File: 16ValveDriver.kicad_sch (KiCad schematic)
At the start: 0 parts

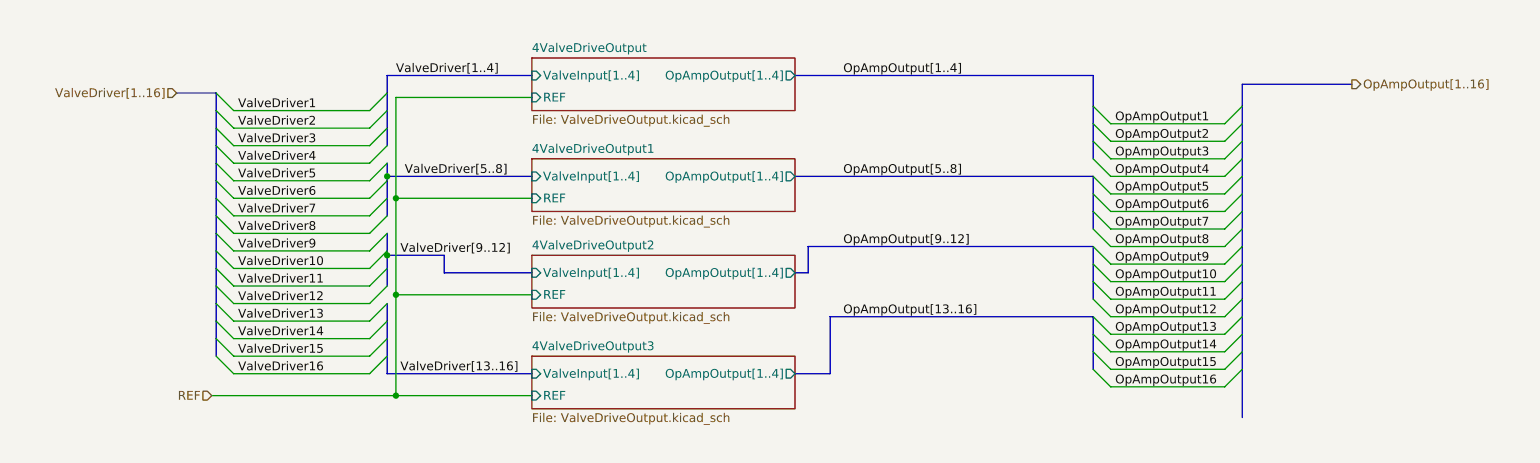
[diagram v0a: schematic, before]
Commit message: Layout p2, fix Analog VCC and GND for opamp circuit
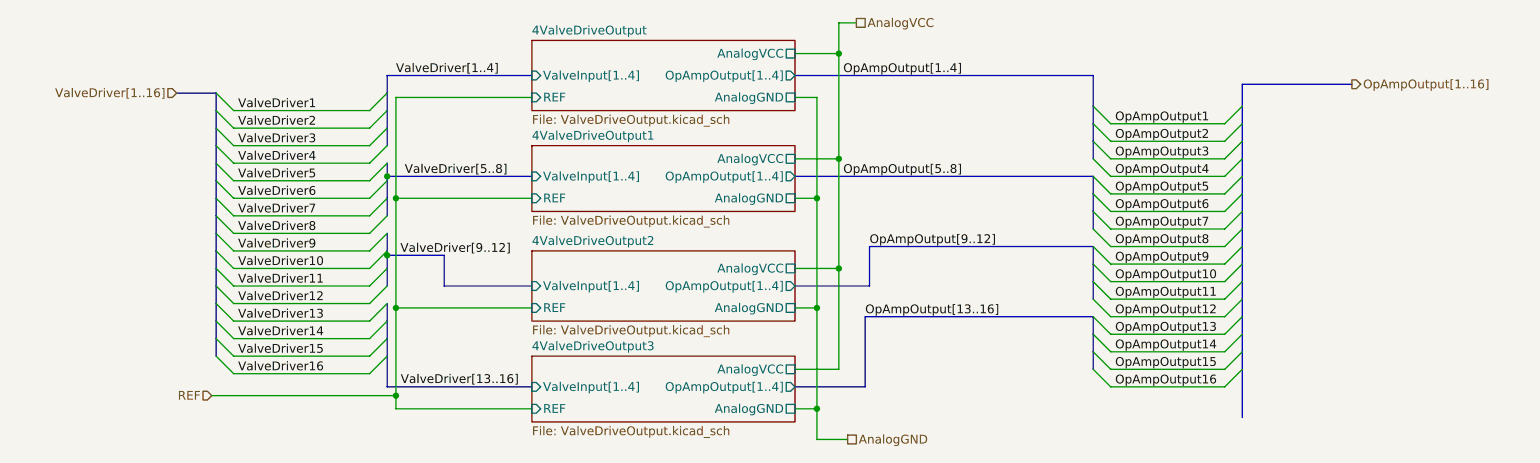
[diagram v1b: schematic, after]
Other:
- sheet 4ValveDriveOutput ports: added AnalogGND, AnalogVCC; removed none
- sheet 4ValveDriveOutput1 ports: added AnalogGND, AnalogVCC; removed none
- sheet 4ValveDriveOutput2 ports: added AnalogGND, AnalogVCC; removed none
- sheet 4ValveDriveOutput3 ports: added AnalogGND, AnalogVCC; removed none

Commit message: Complete layout, HW685 not layout yet
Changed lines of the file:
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@@
+	)
+	(junction
+		(at 87.63 77.47)
+		(diameter 0)
+		(color 0 0 0 0)
 	)
 	(junction
@@
 		)
 	)
+	(bus
+		(pts
+			(xy 87.63 75.565) (xy 87.63 77.47)
+		)
+		(stroke
+			(width 0)
+			(type default)
+		)
+	)
 	(wire
 		(pts
@@
 		)
 	)
-	(bus
-		(pts
-			(xy 85.09 77.47) (xy 106.045 77.47)
-		)
-		(stroke
-			(width 0)
-			(type default)
-		)
-	)
 	(wire
 		(pts
@@
 	(bus
 		(pts
+			(xy 85.09 77.47) (xy 87.63 77.47)
+		)
+		(stroke
+			(width 0)
+			(type default)
+		)
+	)
+	(bus
+		(pts
 			(xy 187.325 32.385) (xy 187.325 36.83)
 		)
@@
 		(pts
 			(xy 208.915 41.91) (xy 208.915 44.45)
+		)
+		(stroke
+			(width 0)
+			(type default)
+		)
+	)
+	(bus
+		(pts
+			(xy 87.63 77.47) (xy 106.045 77.47)
 		)
 		(stroke
@@
 	)
 	(label "ValveDriver[13..16]"
-		(at 87.0509 77.4106 0)
+		(at 87.63 75.565 0)
 		(fields_autoplaced yes)
 		(effects
